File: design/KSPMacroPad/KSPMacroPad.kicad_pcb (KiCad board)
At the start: 2 copper layers, 91 x 107.5 mm, 70 parts, among them SW1 SW_Push, SW10 SW_Push, SW11 SW_Push, SW12 SW_Push, SW13 SW_Push, SW14 SW_Push, SW15 SW_Push, SW16 SW_Push, SW17 RotaryEncoder_Switch, SW18 RotaryEncoder_Switch, SW2 SW_Push, SW3 SW_Push, SW4 SW_Push, SW5 SW_Push, SW6 SW_Push, SW7 SW_Push, SW8 SW_Push, SW9 SW_Push, U1 MOUDLE-SEEEDUINO-XIAO

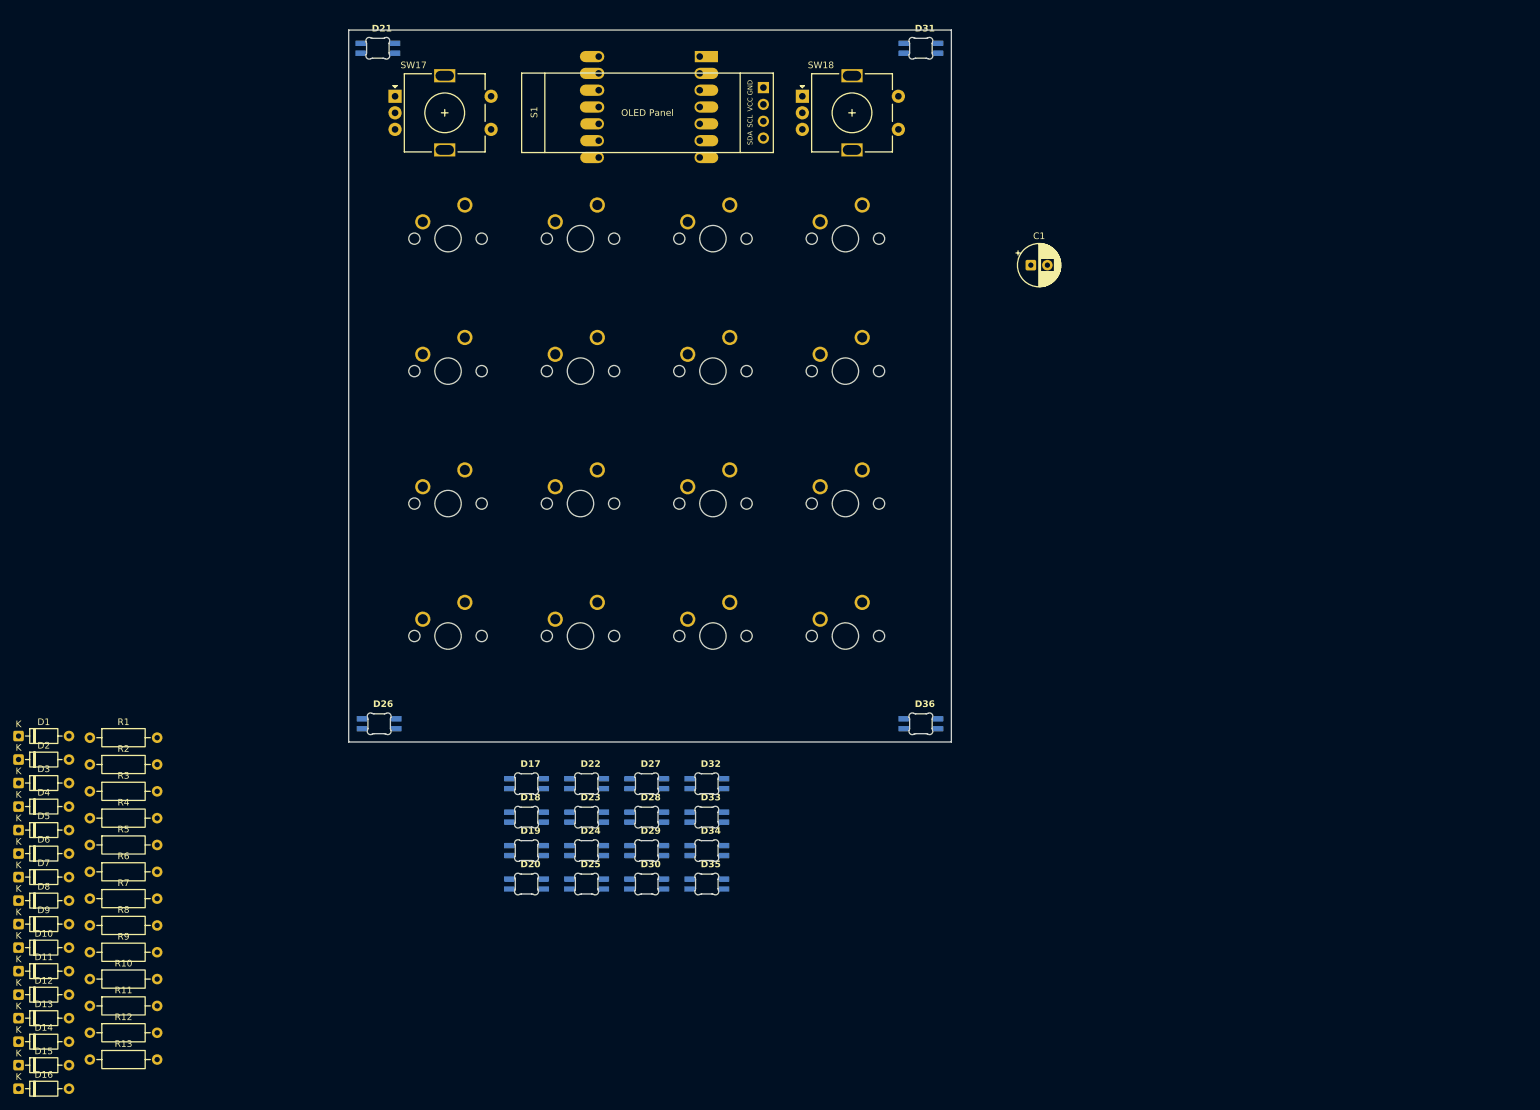
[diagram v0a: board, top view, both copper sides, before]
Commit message: backup KSPMacroPad.kicad_pcb
doing some schematic fixes and I want to make sure the PCB is backed up before I align it to the schematic fixes
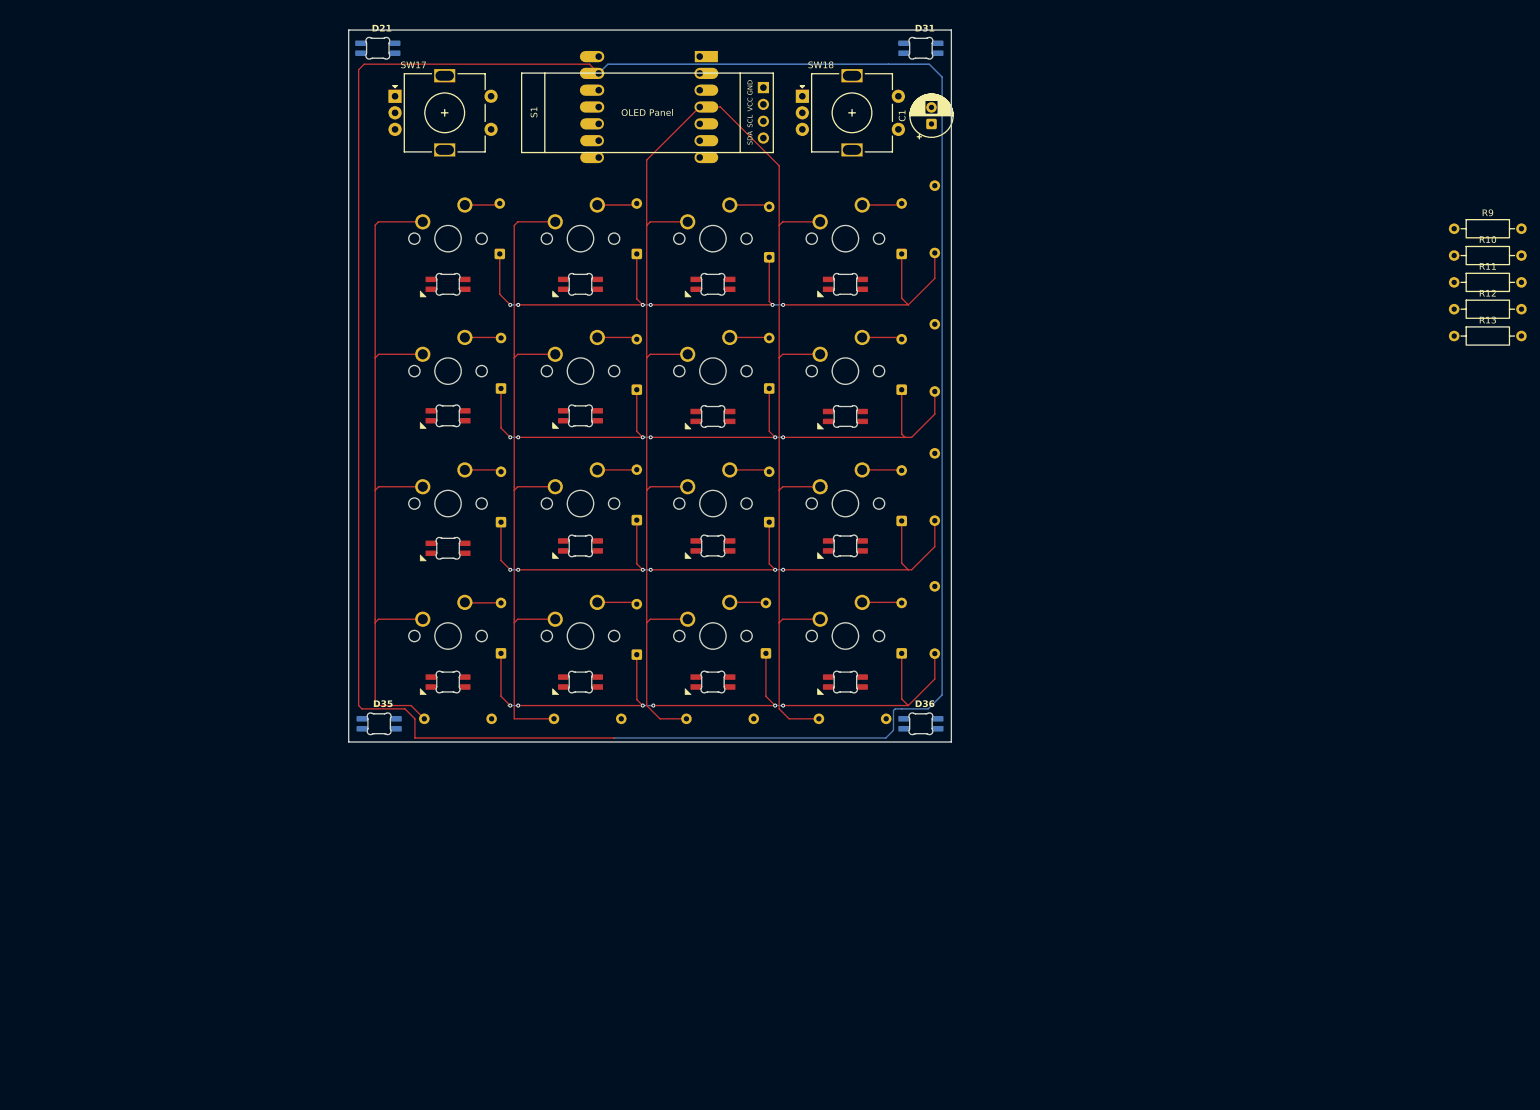
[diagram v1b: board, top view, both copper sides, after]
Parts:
- D1, D17, D18, D19, D2, D20, D22, D23, D24, D25, D26, D27, D28, D29, D3, D30, D32, D33, D34, D4, R1, R2, R3, R4, R5, R6, R7, R8: moved to B.Cu
- D10: renamed from D11; moved to B.Cu
- D11: renamed from D12; moved to B.Cu
- D12: renamed from D5; moved to B.Cu
- D13: renamed from D6; moved to B.Cu
- D14: renamed from D7; moved to B.Cu
- D15: renamed from D8; moved to B.Cu
- D16: renamed from D9; moved to B.Cu
- D5: renamed from D14; moved to B.Cu
- D6: renamed from D13; moved to B.Cu
- D7: renamed from D15; moved to B.Cu
- D8: renamed from D16; moved to B.Cu
- D9: renamed from D10; moved to B.Cu
- moved R10 233.2 mm to (236.9, 67.5)
- moved R11 233.2 mm to (236.9, 71.6)
- moved R12 233.2 mm to (236.9, 75.7)
- moved R13 233.2 mm to (236.9, 79.7)
- moved R9 233.2 mm to (236.9, 63.5)
- moved R8 163.1 mm to (158.5, 67.2), turned to 90 degrees
- moved D13 161.2 mm to (153.5, 67.3), turned to 90 degrees
- moved D9 154.0 mm to (133.5, 67.8), turned to 90 degrees
- moved D14 152.3 mm to (153.5, 87.8), turned to 90 degrees
- moved D5 151.2 mm to (113.5, 67.3), turned to 90 degrees
- moved R7 148.8 mm to (158.5, 88.1), turned to 90 degrees
- moved D15 145.2 mm to (153.5, 107.6), turned to 90 degrees
- moved D10 143.5 mm to (133.5, 87.6), turned to 90 degrees
- moved D16 139.5 mm to (153.5, 127.6), turned to 90 degrees
- moved R6 138.2 mm to (158.5, 107.6), turned to 90 degrees
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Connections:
- R9 pad 2: /ROW1 -> Net-(U1-PA02_A0_D0)
- U1 pad 1: /ROW1 -> Net-(U1-PA02_A0_D0)
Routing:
- net /GND: track 0.00 -> 376.9 mm
- net /COL3: track 0.00 -> 256.1 mm
- net /COL1: track 0.00 -> 216.6 mm
- net /ROW3: track 0.00 -> 203.8 mm, vias 0 -> 12
- net /ROW1: track 0.00 -> 201.2 mm, vias 0 -> 12
- net Net-(D14-A): track 0.00 -> 6.07 mm
- net Net-(D8-A): track 0.00 -> 6.07 mm
- net Net-(D6-A): track 0.00 -> 6.07 mm
- net Net-(D9-A): track 0.00 -> 6.07 mm
- net Net-(D11-A): track 0.00 -> 6.07 mm
- net Net-(D13-A): track 0.00 -> 6.06 mm
- net Net-(D5-A): track 0.00 -> 6.06 mm
- net Net-(D4-A): track 0.00 -> 6.03 mm
- net Net-(D16-A): track 0.00 -> 5.99 mm
- net Net-(D15-A): track 0.00 -> 5.99 mm
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
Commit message: all components laid out
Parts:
- added NT1: NetTie_2, NetTie:NetTie-2_SMD_Pad0.5mm, F.Cu at (103.5, 39.5)
- added NT2: NetTie_2, NetTie:NetTie-2_SMD_Pad0.5mm, F.Cu at (103.5, 37.5)
- C1, R10, R11, R12, R13, R9: moved to B.Cu
- LED14: renamed from D31; moved to B.Cu
- LED17: renamed from D33; moved to F.Cu
- LED18: renamed from D34; moved to F.Cu
- LED8: renamed from D21; moved to B.Cu
- moved R13 165.2 mm to (73.0, 59.5), turned to 90 degrees
- moved R11 112.1 mm to (128.5, 43.0), turned to -90 degrees
- moved R12 106.6 mm to (135.5, 42.9), turned to -90 degrees
- moved R10 102.0 mm to (138.7, 40.0), turned to 180 degrees
- moved R9 101.8 mm to (138.7, 37.0), turned to 180 degrees
- moved LED8 100.5 mm to (105.0, 132.1), turned to 180 degrees
- moved LED17 89.7 mm to (74.6, 36.4), turned to 0 degrees
- moved C1 84.0 mm to (74.0, 45.5)
- moved LED18 75.9 mm to (156.5, 36.5), turned to 0 degrees
- moved LED9 63.3 mm to (125.0, 72.0)
- moved LED14 56.7 mm to (145.0, 91.9), turned to 180 degrees
- moved LED10 44.9 mm to (125.0, 91.9)
- moved LED12 40.1 mm to (125.0, 132.1)
- moved LED11 39.9 mm to (125.0, 111.9)
- moved LED7 39.9 mm to (105.0, 111.9)
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- renumbered D17 to LED1, D26 to LED10, D27 to LED11, D28 to LED12, D32 to LED13, D30 to LED15, D29 to LED16, D35 to LED19, D18 to LED2, D36 to LED20, D19 to LED3, D20 to LED4, D24 to LED5, D23 to LED6, D22 to LED7, D25 to LED9
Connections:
- C1 pad 1: /5V -> /LED_5V
- C1 pad 2: /GND -> /LED_GND
- D1 pad 1: /ROW1 -> Net-(D1-K)
- D10 pad 1: /ROW1 -> Net-(D10-K)
- D11 pad 1: /ROW3 -> Net-(D11-K)
- D12 pad 1: /ROW3 -> Net-(D12-K)
- D13 pad 1: /ROW1 -> Net-(D1-K)
- D14 pad 1: /ROW1 -> Net-(D10-K)
- D15 pad 1: /ROW3 -> Net-(D11-K)
- D16 pad 1: /ROW3 -> Net-(D12-K)
- D2 pad 1: /ROW1 -> Net-(D10-K)
- D3 pad 1: /ROW3 -> Net-(D11-K)
- D4 pad 1: /ROW3 -> Net-(D12-K)
- D5 pad 1: /ROW1 -> Net-(D1-K)
- D6 pad 1: /ROW1 -> Net-(D10-K)
- D7 pad 1: /ROW3 -> Net-(D11-K)
- D8 pad 1: /ROW3 -> Net-(D12-K)
- D9 pad 1: /ROW1 -> Net-(D1-K)
- LED1 pad 1: unconnected-(D17-VSS-Pad1) -> /LED_GND
- LED1 pad 2: Net-(D17-DIN) -> Net-(LED1-DIN)
- LED1 pad 3: /5V -> /LED_5V
- LED10 pad 1: /GND -> /LED_GND
- LED10 pad 2: Net-(D23-DOUT) -> Net-(LED10-DIN)
- LED10 pad 3: /5V -> /LED_5V
- LED10 pad 4: Net-(D26-DOUT) -> Net-(LED10-DOUT)
- LED11 pad 1: /GND -> /LED_GND
- LED11 pad 3: /5V -> /LED_5V
- LED12 pad 1: /GND -> /LED_GND
- LED12 pad 2: Net-(D21-DOUT) -> Net-(LED12-DIN)
- LED12 pad 3: /5V -> /LED_5V
- LED12 pad 4: Net-(D28-DOUT) -> Net-(LED12-DOUT)
- LED13 pad 1: /GND -> /LED_GND
- LED13 pad 3: /5V -> /LED_5V
- LED13 pad 4: unconnected-(D32-DOUT-Pad4) -> Net-(LED13-DOUT)
- LED14 pad 1: /GND -> /LED_GND
- LED14 pad 2: Net-(D26-DOUT) -> Net-(LED14-DIN)
- LED14 pad 3: /5V -> /LED_5V
- LED14 pad 4: Net-(D17-DIN) -> Net-(LED10-DIN)
- LED15 pad 1: /GND -> /LED_GND
- LED15 pad 3: /5V -> /LED_5V
- LED15 pad 4: Net-(D18-DIN) -> Net-(LED15-DOUT)
- LED16 pad 1: /GND -> /LED_GND
- LED16 pad 2: Net-(D28-DOUT) -> Net-(LED15-DOUT)
- LED16 pad 3: /5V -> /LED_5V
- LED16 pad 4: Net-(D19-DIN) -> Net-(LED12-DIN)
- LED17 pad 1: /GND -> /LED_GND
- LED17 pad 2: Net-(D33-DIN) -> Net-(LED17-DIN)
- LED17 pad 3: /5V -> /LED_5V
- LED17 pad 4: Net-(D33-DOUT) -> Net-(LED1-DIN)
- LED18 pad 1: /GND -> /LED_GND
- LED18 pad 2: Net-(D33-DOUT) -> Net-(LED13-DOUT)
- LED18 pad 3: /5V -> /LED_5V
- LED18 pad 4: Net-(D34-DOUT) -> Net-(LED14-DIN)
- LED19 pad 1: /GND -> /LED_GND
- LED19 pad 2: Net-(D34-DOUT) -> Net-(LED19-DIN)
- LED19 pad 3: /5V -> /LED_5V
- LED2 pad 1: /GND -> /LED_GND
- LED2 pad 2: Net-(D18-DIN) -> Net-(LED2-DIN)
- LED2 pad 3: /5V -> /LED_5V
- LED2 pad 4: Net-(D18-DOUT) -> Net-(LED2-DOUT)
- LED20 pad 1: /GND -> /LED_GND
- LED20 pad 3: /5V -> /LED_5V
- LED20 pad 4: Net-(D20-DIN) -> unconnected-(LED20-DOUT-Pad4)
- LED3 pad 1: /GND -> /LED_GND
- LED3 pad 2: Net-(D19-DIN) -> Net-(LED2-DOUT)
- LED3 pad 3: /5V -> /LED_5V
- LED4 pad 1: /GND -> /LED_GND
- LED4 pad 2: Net-(D20-DIN) -> Net-(LED4-DIN)
- LED4 pad 3: /5V -> /LED_5V
- LED4 pad 4: Net-(D20-DOUT) -> Net-(LED19-DIN)
- LED5 pad 1: /GND -> /LED_GND
- LED5 pad 3: /5V -> /LED_5V
- LED6 pad 1: /GND -> /LED_GND
- LED6 pad 2: Net-(D18-DOUT) -> Net-(LED10-DOUT)
- LED6 pad 3: /5V -> /LED_5V
- LED6 pad 4: Net-(D23-DOUT) -> Net-(LED2-DIN)
- LED7 pad 1: /GND -> /LED_GND
- LED7 pad 3: /5V -> /LED_5V
- LED8 pad 1: /GND -> /LED_GND
- LED8 pad 2: Net-(D20-DOUT) -> Net-(LED12-DOUT)
- LED8 pad 3: /5V -> /LED_5V
- LED8 pad 4: Net-(D21-DOUT) -> Net-(LED4-DIN)
- LED9 pad 1: /GND -> /LED_GND
- LED9 pad 3: /5V -> /LED_5V
- R1 pad 1: /COL1 -> Net-(R1-Pad1)
- R1 pad 2: /3.3V -> /col1_2
- R10 pad 1: /GND -> /an_GND
- R10 pad 2: /ROW3 -> /row3_4
- R11 pad 1: /GND -> /an_GND
- R11 pad 2: /COL1 -> /col1_2
- R12 pad 1: /COL3 -> /an_GND
- R12 pad 2: /GND -> /col3_4
- R13 pad 1: Net-(U1-PB08_A6_D6_TX) -> Net-(LED17-DIN)
- R13 pad 2: Net-(D33-DIN) -> Net-(U1-PB08_A6_D6_TX)
- R2 pad 1: /COL1 -> Net-(R2-Pad1)
- R2 pad 2: /3.3V -> /col1_2
- R3 pad 1: /COL3 -> Net-(R3-Pad1)
- R3 pad 2: /3.3V -> /col3_4
- R4 pad 1: /COL3 -> Net-(R4-Pad1)
- R4 pad 2: /3.3V -> /col3_4
- R5 pad 1: /ROW3 -> Net-(D12-K)
- R5 pad 2: /3.3V -> /row3_4
- R6 pad 1: /ROW3 -> Net-(D11-K)
- R6 pad 2: /3.3V -> /row3_4
- R7 pad 1: /ROW1 -> Net-(D10-K)
- R7 pad 2: /3.3V -> /row1_2
- R8 pad 1: /ROW1 -> Net-(D1-K)
- R8 pad 2: /3.3V -> /row1_2
- R9 pad 1: /GND -> /an_GND
- R9 pad 2: Net-(U1-PA02_A0_D0) -> /row1_2
- S1 pad 1: /GND -> /an_GND
- S1 pad 2: /3.3V -> Net-(S1-VCC)
- SW1 pad 1: /COL1 -> Net-(R1-Pad1)
- SW10 pad 1: /COL3 -> Net-(R3-Pad1)
- SW11 pad 1: /COL3 -> Net-(R3-Pad1)
- SW12 pad 1: /COL3 -> Net-(R3-Pad1)
- SW13 pad 1: /COL3 -> Net-(R4-Pad1)
- SW14 pad 1: /COL3 -> Net-(R4-Pad1)
- SW15 pad 1: /COL3 -> Net-(R4-Pad1)
- SW16 pad 1: /COL3 -> Net-(R4-Pad1)
- SW17 pad C: /GND -> /an_GND
- SW18 pad A: Net-(U1-PA7_A8_D8_SCK) -> Net-(U1-PB09_A7_D7_RX)
- SW18 pad B: Net-(U1-PB09_A7_D7_RX) -> /LED_GND
- SW18 pad C: /GND -> /an_GND
- SW2 pad 1: /COL1 -> Net-(R1-Pad1)
- SW3 pad 1: /COL1 -> Net-(R1-Pad1)
- SW4 pad 1: /COL1 -> Net-(R1-Pad1)
- SW5 pad 1: /COL1 -> Net-(R2-Pad1)
- SW6 pad 1: /COL1 -> Net-(R2-Pad1)
- SW7 pad 1: /COL1 -> Net-(R2-Pad1)
- SW8 pad 1: /COL1 -> Net-(R2-Pad1)
- SW9 pad 1: /COL3 -> Net-(R3-Pad1)
- U1 pad 1: Net-(U1-PA02_A0_D0) -> /row1_2
- U1 pad 12: /3.3V -> Net-(S1-VCC)
- U1 pad 13: /GND -> /an_GND
- U1 pad 2: /ROW3 -> /row3_4
- U1 pad 3: /COL1 -> /col1_2
- U1 pad 4: /COL3 -> /col3_4
- U1 pad 9: Net-(U1-PA7_A8_D8_SCK) -> /LED_GND
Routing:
- net /GND: track 376.9 -> 0.00 mm
- net /col3_4: track 0.00 -> 256.1 mm
- net /COL3: track 256.1 -> 0.00 mm
- net /COL1: track 216.6 -> 0.00 mm
- net /ROW3: track 203.8 -> 0.00 mm, vias 12 -> 0
- net /ROW1: track 201.2 -> 0.00 mm, vias 12 -> 0
- net Net-(R1-Pad1): track 0.00 -> 110.4 mm
- net Net-(R2-Pad1): track 0.00 -> 106.2 mm
- net Net-(D12-K): track 0.00 -> 102.9 mm, vias 0 -> 6
- net Net-(D1-K): track 0.00 -> 101.5 mm, vias 0 -> 6
- net Net-(D11-K): track 0.00 -> 100.6 mm, vias 0 -> 6
- net Net-(D10-K): track 0.00 -> 99.6 mm, vias 0 -> 6

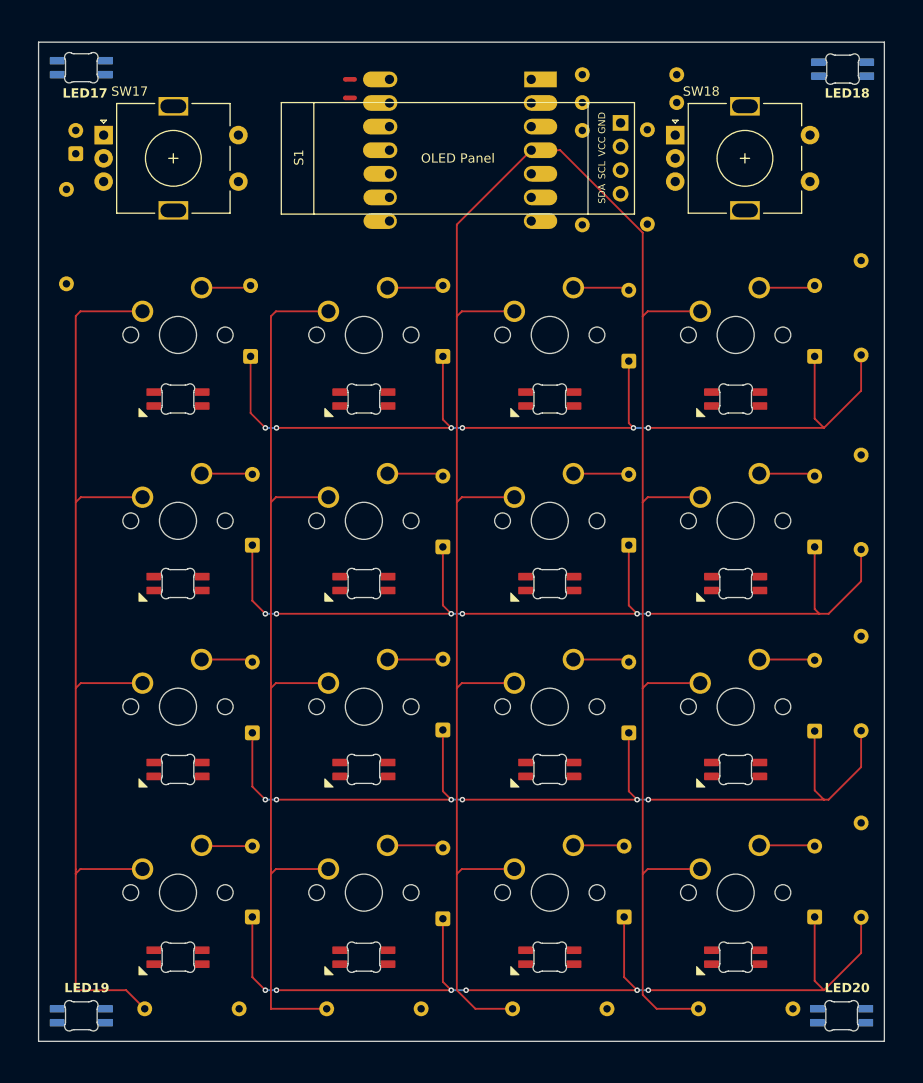
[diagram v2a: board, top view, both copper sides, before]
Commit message: finished PCB
routed everything using the FreeRouting plugin, then cleaned up what it couldn't do. I think everything is wired correctly
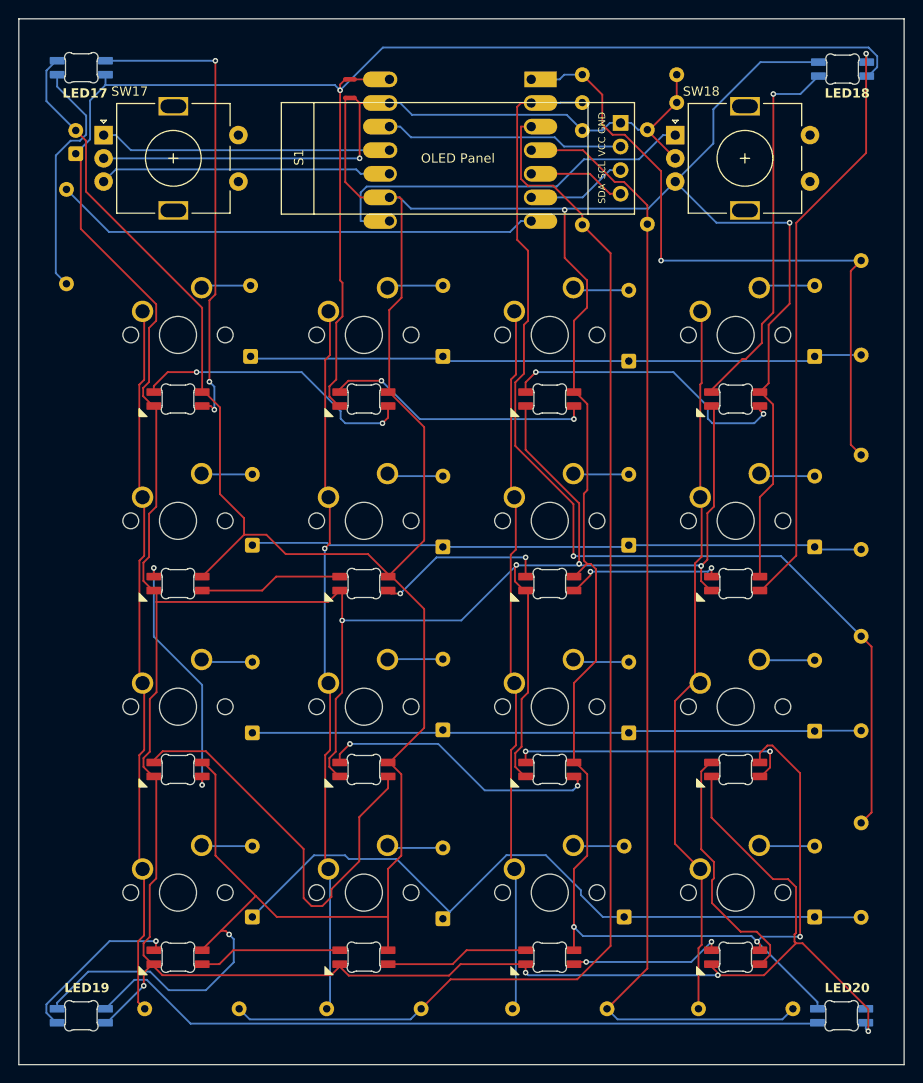
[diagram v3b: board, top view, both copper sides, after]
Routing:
- net /LED_GND: track 0.00 -> 515.1 mm, vias 0 -> 6
- net /LED_5V: track 0.00 -> 498.6 mm, vias 0 -> 9
- net /col1_2: track 0.00 -> 138.6 mm
- net /col3_4: track 256.1 -> 124.1 mm
- net /row3_4: track 0.00 -> 114.7 mm, vias 0 -> 1
- net Net-(LED19-DOUT): track 0.00 -> 79.9 mm
- net Net-(R4-Pad1): track 0.00 -> 78.7 mm
- net /an_GND: track 0.00 -> 78.7 mm, vias 0 -> 1
- net Net-(R3-Pad1): track 0.00 -> 76.6 mm
- net /row1_2: track 0.00 -> 73.3 mm, vias 0 -> 1
- net Net-(LED14-DIN): track 0.00 -> 63.5 mm, vias 0 -> 1
- net Net-(U1-PB08_A6_D6_TX): track 0.00 -> 52.4 mm
- net Net-(LED1-DIN): track 0.00 -> 51.3 mm, vias 0 -> 3
- net Net-(LED3-DOUT): track 0.00 -> 45.7 mm
- net Net-(U1-PB09_A7_D7_RX): track 0.00 -> 42.6 mm
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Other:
- board size 91 x 107.5 mm -> 95.2 x 112.5 mm
